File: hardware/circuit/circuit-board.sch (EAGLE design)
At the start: 9 parts, among them U1 ADUM1200CRZ

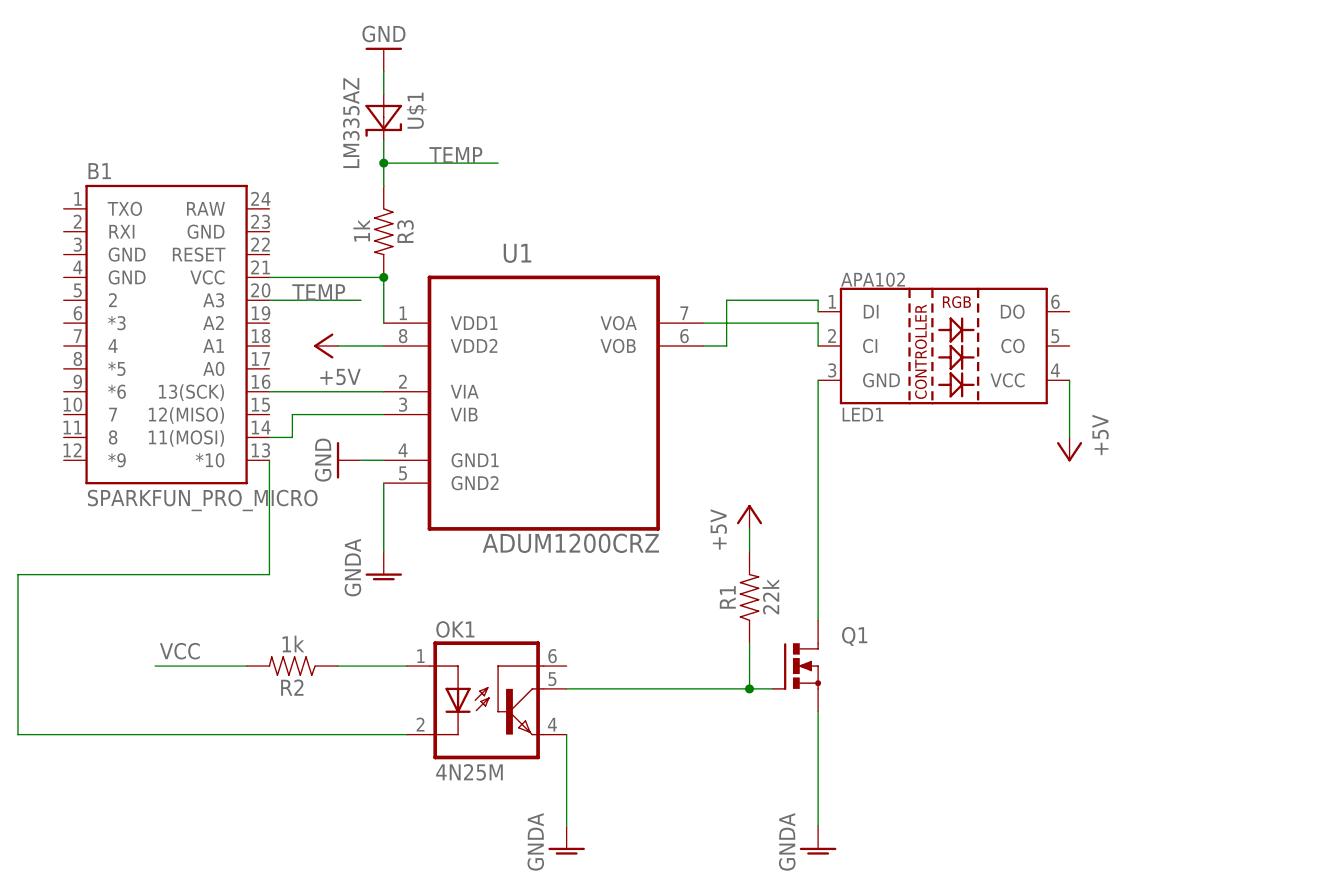
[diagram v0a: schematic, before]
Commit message: Added PN2222A to circuit - disconnects GND2 from ADUM1285CRZ so that current won't leak through the signal lines from the LED strip (LED strip wouldn't power off)
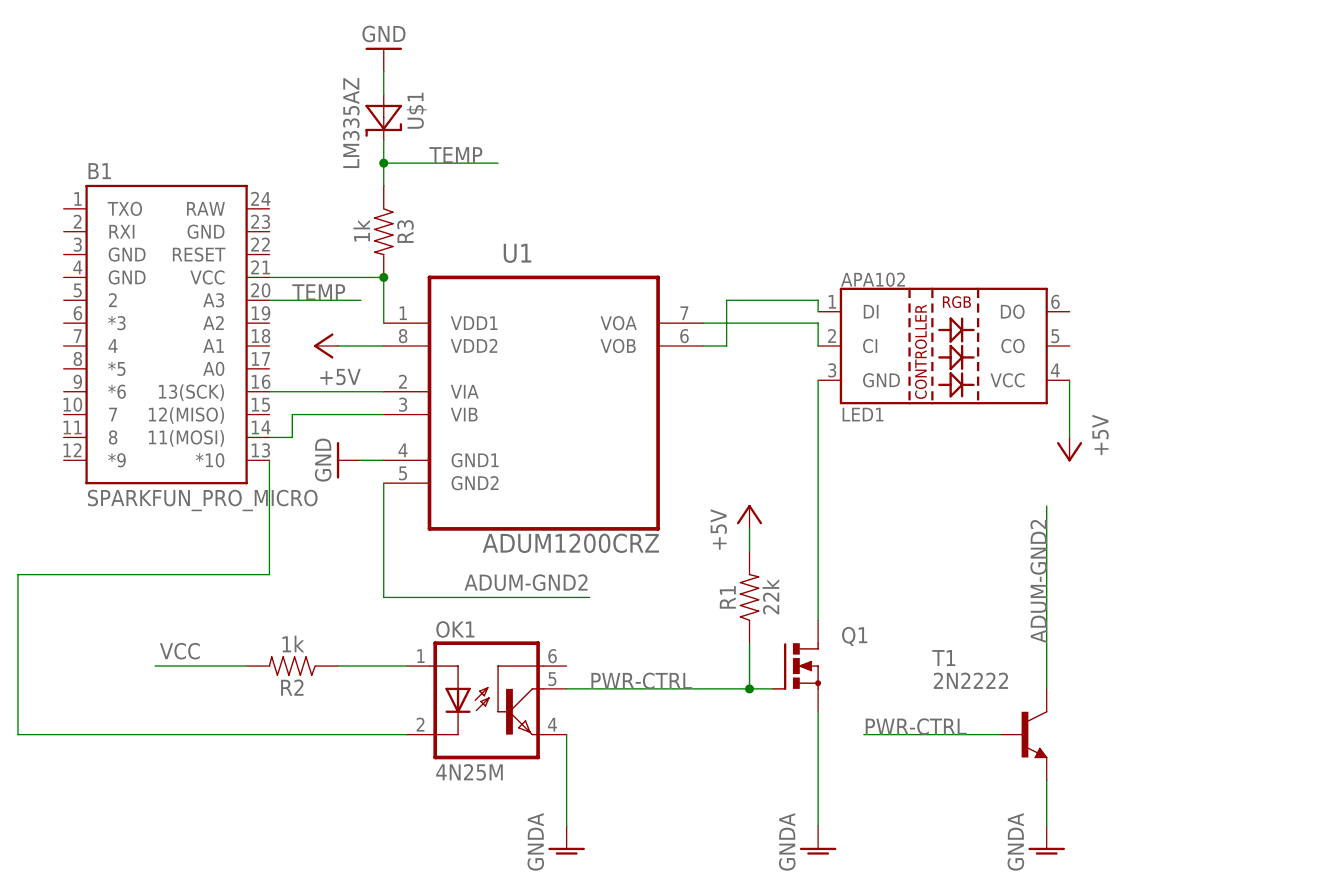
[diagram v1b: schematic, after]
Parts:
- added T1: 2N2222, adafruit:2N2222
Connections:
- removed net N$2: OK1.COL, Q1.G, R1.1
- new net ADUM-GND2: T1.C, U1.GND2
- new net PWR-CTRL: OK1.COL, Q1.G, R1.1, T1.B
- net GNDA: now also T1.E; no longer U1.GND2
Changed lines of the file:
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@@
 <layer number="230" name="230bmp" color="7" fill="1" visible="yes" active="yes"/>
 <layer number="231" name="231bmp" color="7" fill="1" visible="yes" active="yes"/>
+<layer number="232" name="Eagle3D_PG2" color="7" fill="1" visible="no" active="no"/>
+<layer number="233" name="Eagle3D_PG3" color="7" fill="1" visible="no" active="no"/>
 <layer number="248" name="Housing" color="7" fill="1" visible="yes" active="yes"/>
 <layer number="249" name="Edge" color="7" fill="1" visible="yes" active="yes"/>
@@
 <part name="GND1" library="supply1" deviceset="GND" device=""/>
 <part name="R3" library="SparkFun-Resistors" deviceset="1KOHM" device="-0603-1/10W-1%" value="1k"/>
+<part name="T1" library="adafruit" deviceset="2N2222" device=""/>
 </parts>
 <sheets>
@@
 <instance part="GND4" gate="1" x="66.04" y="38.1"/>
 <instance part="U1" gate="A" x="35.56" y="91.44"/>
-<instance part="GND5" gate="1" x="17.78" y="68.58"/>
+<instance part="GND5" gate="1" x="91.44" y="38.1"/>
 <instance part="GND6" gate="1" x="12.7" y="81.28" rot="R270"/>
 <instance part="P+3" gate="1" x="10.16" y="93.98" rot="R90"/>
@@
 <instance part="GND1" gate="1" x="17.78" y="127" rot="R180"/>
 <instance part="R3" gate="G$1" x="17.78" y="106.68" rot="R270"/>
+<instance part="T1" gate="G$1" x="88.9" y="50.8"/>
 </instances>
 <busses>
@@
 </segment>
 <segment>
-<pinref part="U1" gate="A" pin="GND2"/>
-<wire x1="17.78" y1="78.74" x2="17.78" y2="71.12" width="0.1524" layer="91"/>
+<pinref part="T1" gate="G$1" pin="E"/>
 <pinref part="GND5" gate="1" pin="GNDA"/>
+<wire x1="91.44" y1="40.64" x2="91.44" y2="45.72" width="0.1524" layer="91"/>
 </segment>
 </net>
@@
 </segment>
 </net>
-<net name="N$2" class="0">
+<net name="PWR-CTRL" class="0">
 <segment>
 <pinref part="R1" gate="G$1" pin="1"/>
@@
 <junction x="58.42" y="55.88"/>
 <pinref part="Q1" gate="G$1" pin="G"/>
+<label x="40.64" y="55.88" size="1.778" layer="95"/>
+</segment>
+<segment>
+<pinref part="T1" gate="G$1" pin="B"/>
+<wire x1="86.36" y1="50.8" x2="71.12" y2="50.8" width="0.1524" layer="91"/>
+<label x="71.12" y="50.8" size="1.778" layer="95"/>
 </segment>
 </net>
@@
 </segment>
 </net>
+<net name="ADUM-GND2" class="0">
+<segment>
+<pinref part="U1" gate="A" pin="GND2"/>
+<wire x1="17.78" y1="78.74" x2="17.78" y2="66.04" width="0.1524" layer="91"/>
+<wire x1="17.78" y1="66.04" x2="40.64" y2="66.04" width="0.1524" layer="91"/>
+<label x="40.64" y="68.58" size="1.778" layer="95" rot="R180"/>
+</segment>
+<segment>
+<pinref part="T1" gate="G$1" pin="C"/>
+<wire x1="91.44" y1="55.88" x2="91.44" y2="76.2" width="0.1524" layer="91"/>
+<label x="91.44" y="60.96" size="1.778" layer="95" rot="R90"/>
+</segment>
+</net>

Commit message: Added solder pads to circuit schematic
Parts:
- added LSP1, LSP2: SE14, solpad:SE14
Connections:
- net +5V: now also LSP2.MP
- net GNDA: now also LSP1.MP
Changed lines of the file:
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@@
 <part name="R3" library="SparkFun-Resistors" deviceset="1KOHM" device="-0603-1/10W-1%" value="1k"/>
 <part name="T1" library="adafruit" deviceset="2N2222" device=""/>
+<part name="LSP1" library="solpad" deviceset="SE14" device=""/>
+<part name="LSP2" library="solpad" deviceset="SE14" device=""/>
 </parts>
 <sheets>
@@
 <instance part="R3" gate="G$1" x="17.78" y="106.68" rot="R270"/>
 <instance part="T1" gate="G$1" x="88.9" y="50.8"/>
+<instance part="LSP1" gate="1" x="101.6" y="43.18" rot="R270"/>
+<instance part="LSP2" gate="1" x="104.14" y="86.36" rot="R270"/>
 </instances>
 <busses>
@@
 <pinref part="T1" gate="G$1" pin="E"/>
 <pinref part="GND5" gate="1" pin="GNDA"/>
-<wire x1="91.44" y1="40.64" x2="91.44" y2="45.72" width="0.1524" layer="91"/>
+<wire x1="91.44" y1="40.64" x2="91.44" y2="43.18" width="0.1524" layer="91"/>
+<pinref part="LSP1" gate="1" pin="MP"/>
+<wire x1="91.44" y1="43.18" x2="91.44" y2="45.72" width="0.1524" layer="91"/>
+<wire x1="99.06" y1="43.18" x2="91.44" y2="43.18" width="0.1524" layer="91"/>
+<junction x="91.44" y="43.18"/>
 </segment>
 </net>
@@
 <pinref part="P+1" gate="1" pin="+5V"/>
 <pinref part="LED1" gate="G$1" pin="VCC"/>
-<wire x1="93.98" y1="83.82" x2="93.98" y2="90.17" width="0.1524" layer="91"/>
+<wire x1="93.98" y1="83.82" x2="93.98" y2="86.36" width="0.1524" layer="91"/>
+<pinref part="LSP2" gate="1" pin="MP"/>
+<wire x1="93.98" y1="86.36" x2="93.98" y2="90.17" width="0.1524" layer="91"/>
+<wire x1="101.6" y1="86.36" x2="93.98" y2="86.36" width="0.1524" layer="91"/>
+<junction x="93.98" y="86.36"/>
 </segment>
 <segment>

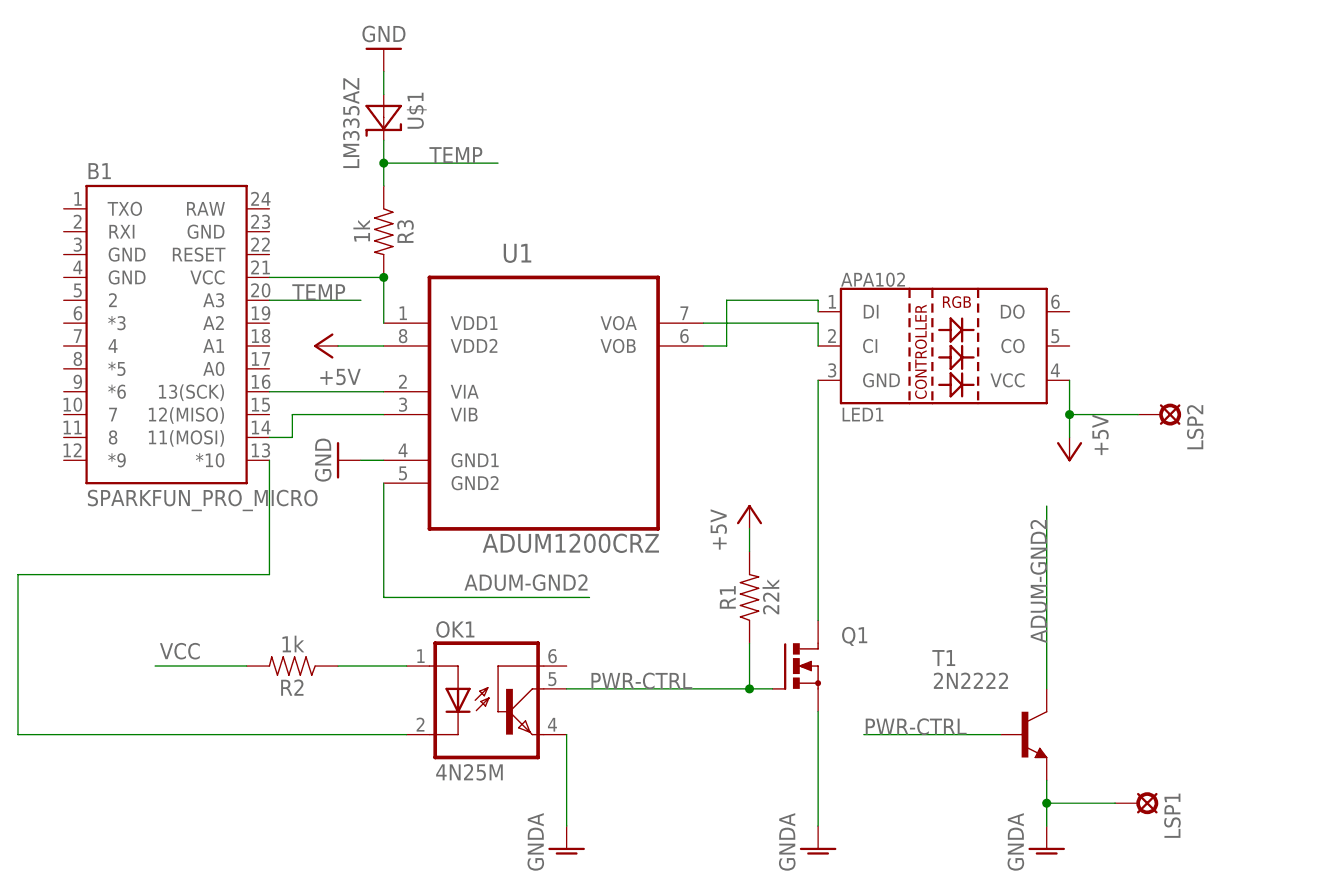
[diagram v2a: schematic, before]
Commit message: Replaced power/signal holes with SMD pads, added initial PCB layout, changed pins for final board
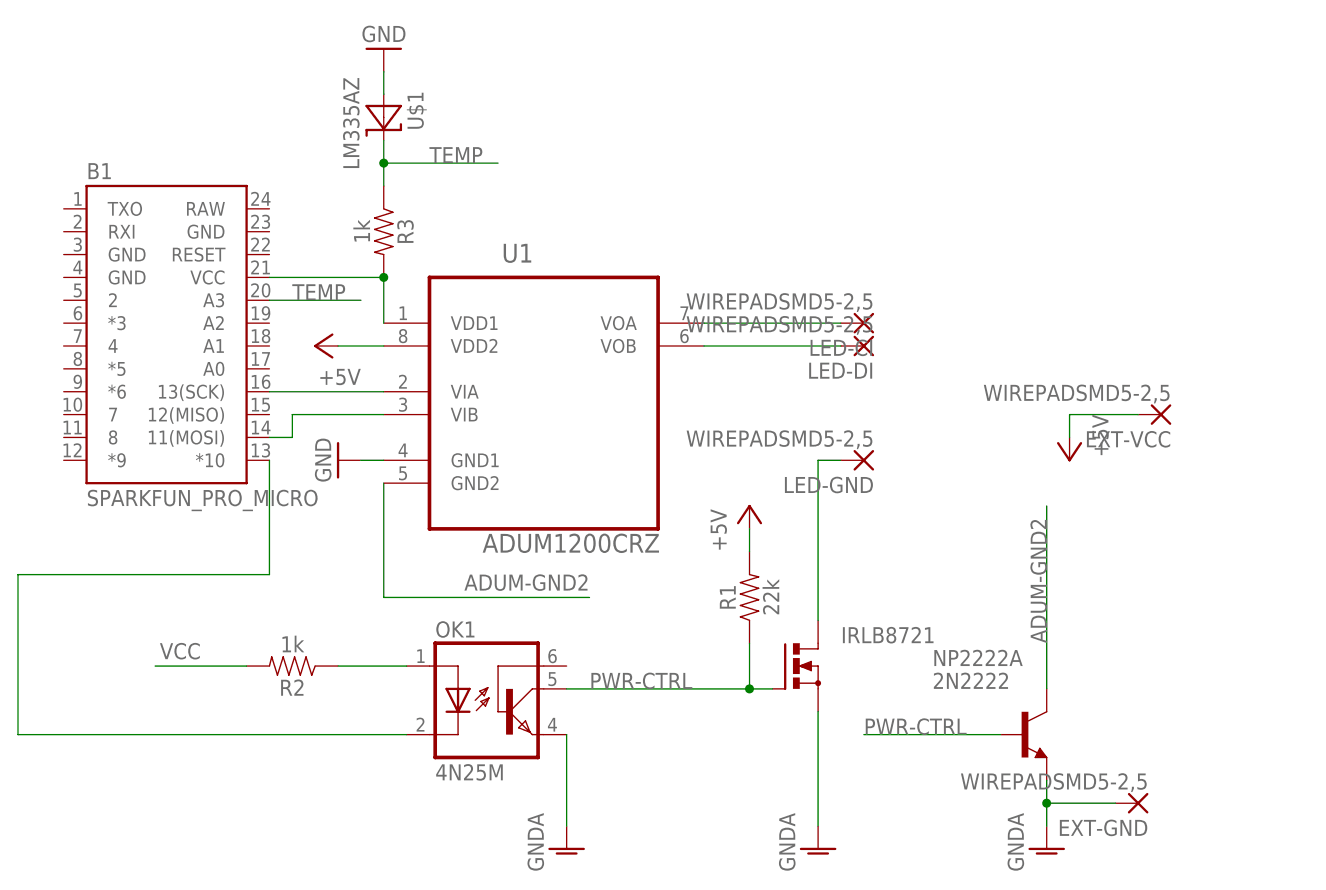
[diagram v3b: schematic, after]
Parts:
- removed LED1: LED-APA102, Ai_LED:LED-APA102
- removed LSP1, LSP2: SE14, solpad:SE14
- added EXT-GND, EXT-VCC, LED-CI, LED-DI, LED-GND: WIREPADSMD5-2,5, wirepad:WIREPADSMD5-2,5
- renumbered Q1 to IRLB8721, T1 to NP2222A
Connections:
- removed net N$9: LED1.DI, U1.VOB
- new net N$1: LED-DI.P, U1.VOB
- net +5V: now also EXT-VCC.P; no longer LED1.VCC, LSP2.MP
- net GNDA: now also EXT-GND.P; no longer LSP1.MP
- net N$3: now also LED-GND.P; no longer LED1.GND
- net N$7: now also LED-CI.P; no longer LED1.CI
